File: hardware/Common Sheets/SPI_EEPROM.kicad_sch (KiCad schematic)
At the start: 3 parts, among them U4 M95320-RMN6

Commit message: Fix swapped pins on digital I/O card, add kibot job
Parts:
- renumbered R26 to R33
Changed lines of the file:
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@@
 		(on_board yes)
 		(dnp no)
-		(property "Reference" "R26"
+		(property "Reference" "R33"
 			(at 111.506 79.756 90)
 			(effects
@@
 			(project "HackerDAQ Voltage Card"
 				(path "/af2d881c-6553-449d-9093-6deb41497bdc/2388c7f7-4514-41da-b315-2dcc3aa57748"
-					(reference "R26")
+					(reference "R33")
 					(unit 1)
 				)

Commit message: Fix DRC/ERC errors
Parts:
- renumbered C31 to C5, U4 to U9
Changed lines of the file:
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@@
 		(dnp no)
 		(fields_autoplaced yes)
-		(property "Reference" "U4"
+		(property "Reference" "U9"
 			(at 96.1233 64.77 0)
 			(effects
@@
 			(project ""
 				(path "/af2d881c-6553-449d-9093-6deb41497bdc/2388c7f7-4514-41da-b315-2dcc3aa57748"
-					(reference "U4")
+					(reference "U9")
 					(unit 1)
 				)
@@
 		(dnp no)
 		(fields_autoplaced yes)
-		(property "Reference" "C31"
+		(property "Reference" "C5"
 			(at 86.36 58.4262 0)
 			(effects
@@
 			(project "HackerDAQ Voltage Card"
 				(path "/af2d881c-6553-449d-9093-6deb41497bdc/2388c7f7-4514-41da-b315-2dcc3aa57748"
-					(reference "C31")
+					(reference "C5")
 					(unit 1)
 				)

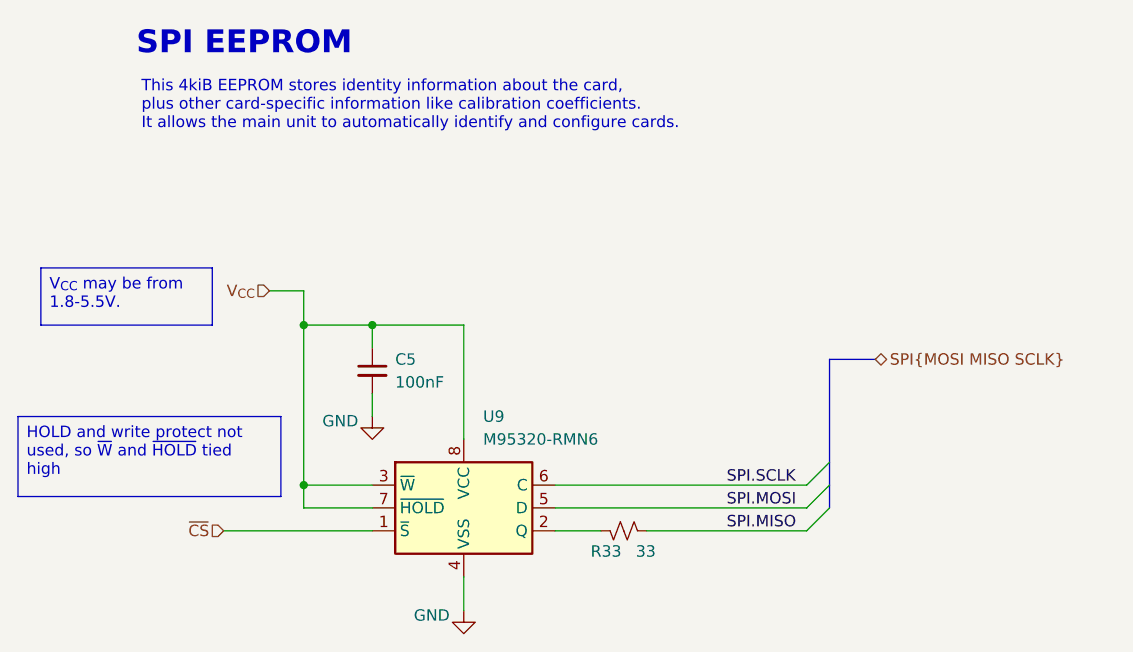
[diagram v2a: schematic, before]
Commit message: Update voltage card to KiCAD 10
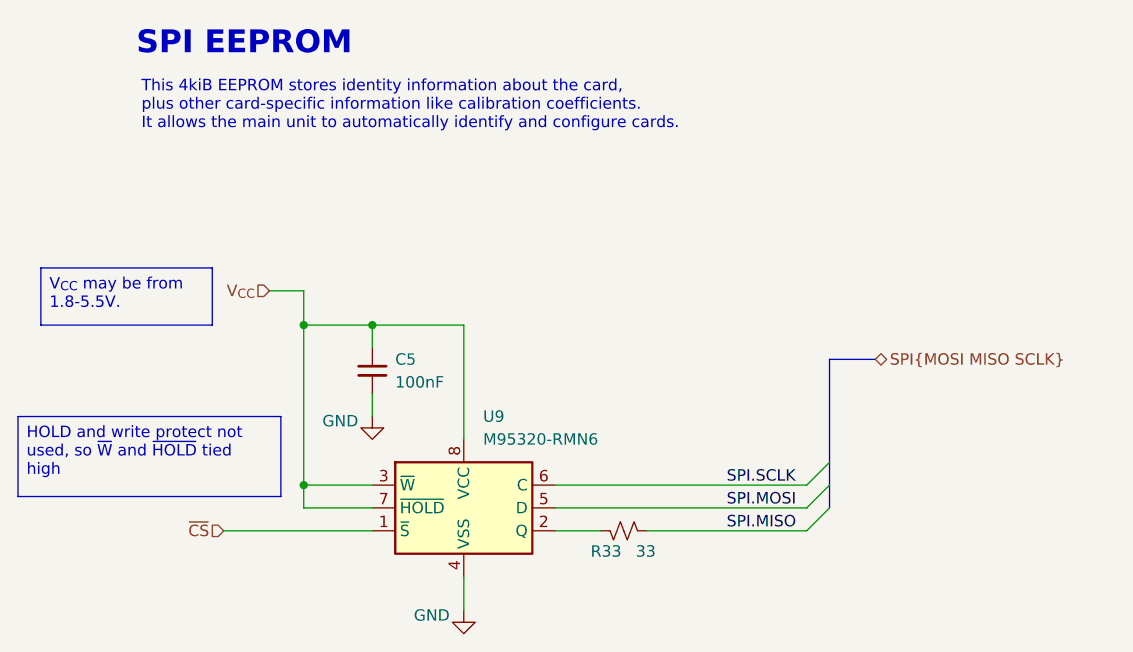
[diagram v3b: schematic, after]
